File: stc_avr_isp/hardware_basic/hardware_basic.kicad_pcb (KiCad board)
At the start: 2 copper layers, 18 x 42.8 mm, 16 parts, among them J1 Conn_01x09_Socket, J2 Conn_01x09_Socket, J3 ISP, J4 BAUD RATE

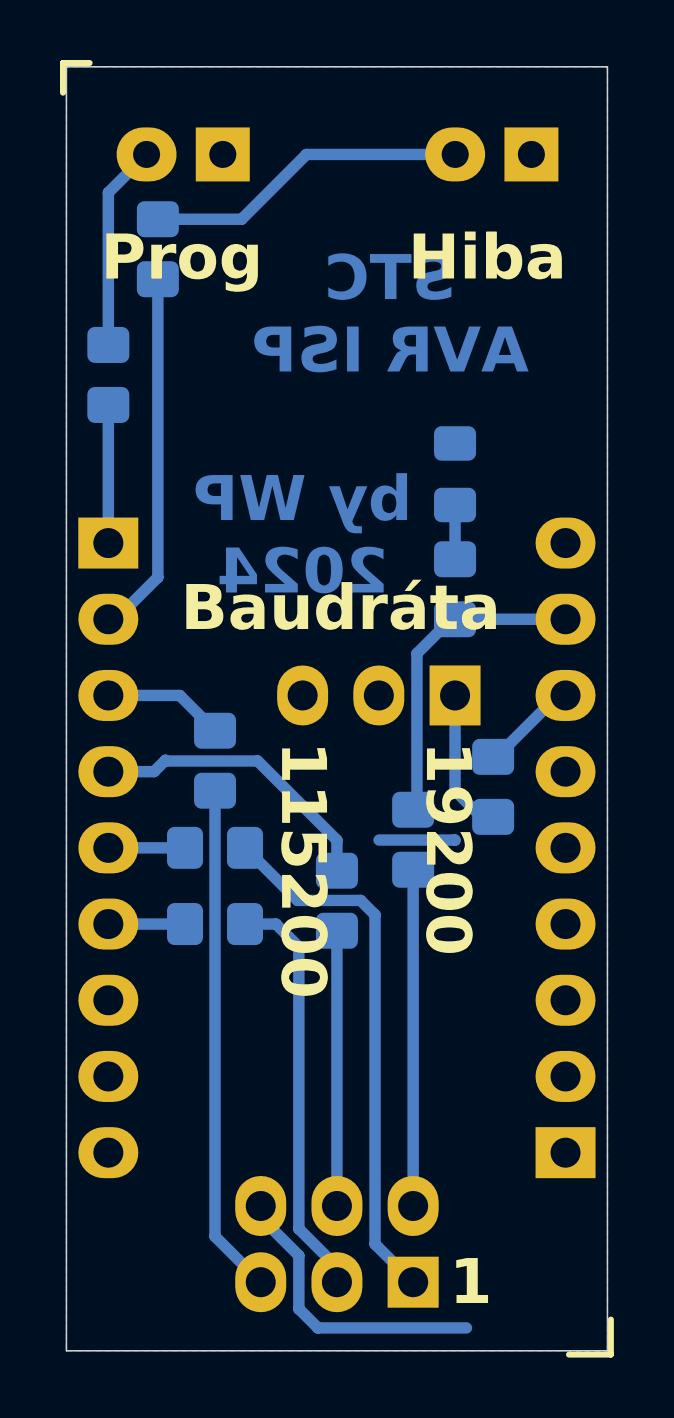
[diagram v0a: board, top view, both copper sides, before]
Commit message: Add fancy blink animation on reset, specify resistor values
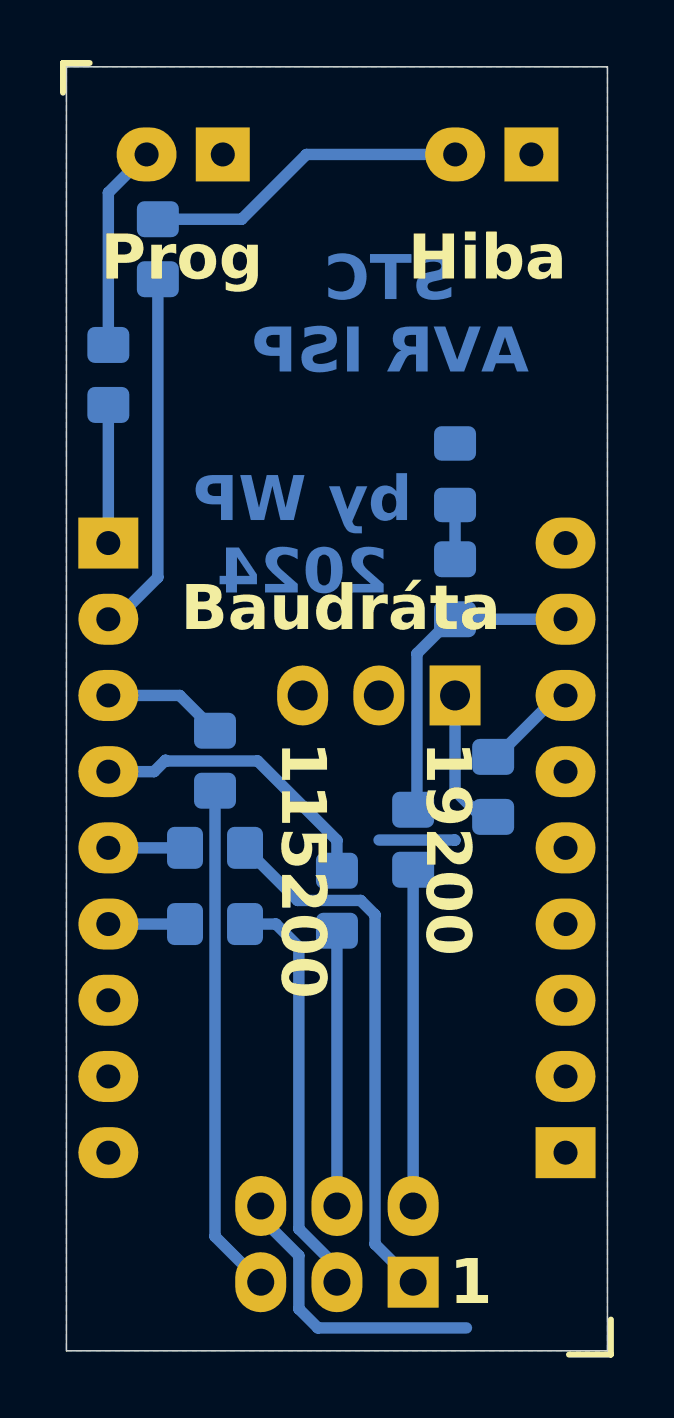
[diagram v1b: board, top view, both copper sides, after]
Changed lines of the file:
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@@
 			(at 0 0 180)
 			(size 1.8 1.8)
-			(drill 0.9)
+			(drill 0.8)
 			(layers "*.Cu" "*.Mask")
 			(remove_unused_layers no)
@@
 			(at 2.54 0 180)
 			(size 2 1.8)
-			(drill 0.9)
+			(drill 0.8)
 			(layers "*.Cu" "*.Mask")
 			(remove_unused_layers no)
@@
 			(at 0 0)
 			(size 2 1.7)
-			(drill 1)
+			(drill 0.8)
 			(layers "*.Cu" "*.Mask")
 			(remove_unused_layers no)
@@
 			(at 0 2.54)
 			(size 2 1.7)
-			(drill 1)
+			(drill 0.8)
 			(layers "*.Cu" "*.Mask")
 			(remove_unused_layers no)
@@
 			(at 0 5.08)
 			(size 2 1.7)
-			(drill 1)
+			(drill 0.8)
 			(layers "*.Cu" "*.Mask")
 			(remove_unused_layers no)
@@
 			(at 0 7.62)
 			(size 2 1.7)
-			(drill 1)
+			(drill 0.8)
 			(layers "*.Cu" "*.Mask")
 			(remove_unused_layers no)
@@
 			(at 0 10.16)
 			(size 2 1.7)
-			(drill 1)
+			(drill 0.8)
 			(layers "*.Cu" "*.Mask")
 			(remove_unused_layers no)
@@
 			(at 0 12.7)
 			(size 2 1.7)
-			(drill 1)
+			(drill 0.8)
 			(layers "*.Cu" "*.Mask")
 			(remove_unused_layers no)
@@
 			(at 0 15.24)
 			(size 2 1.7)
-			(drill 1)
+			(drill 0.8)
 			(layers "*.Cu" "*.Mask")
 			(remove_unused_layers no)
@@
 			(at 0 17.78)
 			(size 2 1.7)
-			(drill 1)
+			(drill 0.8)
 			(layers "*.Cu" "*.Mask")
 			(remove_unused_layers no)
@@
 			(at 0 20.32)
 			(size 2 1.7)
-			(drill 1)
+			(drill 0.8)
 			(layers "*.Cu" "*.Mask")
 			(remove_unused_layers no)
@@
 			(at 0 0 180)
 			(size 2 1.7)
-			(drill 1)
+			(drill 0.8)
 			(layers "*.Cu" "*.Mask")
 			(remove_unused_layers no)
@@
 			(at 0 2.54 180)
 			(size 2 1.7)
-			(drill 1)
+			(drill 0.8)
 			(layers "*.Cu" "*.Mask")
 			(remove_unused_layers no)
@@
 			(at 0 5.08 180)
 			(size 2 1.7)
-			(drill 1)
+			(drill 0.8)
 			(layers "*.Cu" "*.Mask")
 			(remove_unused_layers no)
@@
 			(at 0 7.62 180)
 			(size 2 1.7)
-			(drill 1)
+			(drill 0.8)
 			(layers "*.Cu" "*.Mask")
 			(remove_unused_layers no)
@@
 			(at 0 10.16 180)
 			(size 2 1.7)
-			(drill 1)
+			(drill 0.8)
 			(layers "*.Cu" "*.Mask")
 			(remove_unused_layers no)
@@
 			(at 0 12.7 180)
 			(size 2 1.7)
-			(drill 1)
+			(drill 0.8)
 			(layers "*.Cu" "*.Mask")
 			(remove_unused_layers no)
@@
 			(at 0 15.24 180)
 			(size 2 1.7)
-			(drill 1)
+			(drill 0.8)
 			(layers "*.Cu" "*.Mask")
 			(remove_unused_layers no)
@@
 			(at 0 17.78 180)
 			(size 2 1.7)
-			(drill 1)
+			(drill 0.8)
 			(layers "*.Cu" "*.Mask")
 			(remove_unused_layers no)
@@
 			(at 0 20.32 180)
 			(size 2 1.7)
-			(drill 1)
+			(drill 0.8)
 			(layers "*.Cu" "*.Mask")
 			(remove_unused_layers no)
@@
 			(at 0 0 180)
 			(size 1.8 1.8)
-			(drill 0.9)
+			(drill 0.8)
 			(layers "*.Cu" "*.Mask")
 			(remove_unused_layers no)
@@
 			(at 2.54 0 180)
 			(size 2 1.8)
-			(drill 0.9)
+			(drill 0.8)
 			(layers "*.Cu" "*.Mask")
 			(remove_unused_layers no)
@@
 			(at 0 0 90)
 			(size 2 1.7)
-			(drill 1)
+			(drill 0.9)
 			(layers "*.Cu" "*.Mask")
 			(remove_unused_layers no)
@@
 			(at -2.54 0 90)
 			(size 2 1.7)
-			(drill 1)
+			(drill 0.9)
 			(layers "*.Cu" "*.Mask")
 			(remove_unused_layers no)
@@
 			(at 0 2.54 90)
 			(size 2 1.7)
-			(drill 1)
+			(drill 0.9)
 			(layers "*.Cu" "*.Mask")
 			(remove_unused_layers no)
@@
 			(at -2.54 2.54 90)
 			(size 2 1.7)
-			(drill 1)
+			(drill 0.9)
 			(layers "*.Cu" "*.Mask")
 			(remove_unused_layers no)
@@
 			(at 0 5.08 90)
 			(size 2 1.7)
-			(drill 1)
+			(drill 0.9)
 			(layers "*.Cu" "*.Mask")
 			(remove_unused_layers no)
@@
 			(at -2.54 5.08 90)
 			(size 1.7 1.7)
-			(drill 1)
+			(drill 0.9)
 			(layers "*.Cu" "*.Mask")
 			(remove_unused_layers no)
@@
 		(tags "resistor handsolder")
 		(property "Reference" "R9"
-			(at 0 1.65 270)
+			(at 0 1.65 -90)
 			(layer "B.SilkS")
 			(effects
@@
 		)
 		(property "Value" "330"
-			(at 0 -1.65 270)
+			(at 0 -1.65 -90)
 			(layer "B.Fab")
 			(effects
@@
 		)
 		(fp_text user "${REFERENCE}"
-			(at 0 0 270)
+			(at 0 0 -90)
 			(layer "B.Fab")
 			(effects
@@
 		(tags "resistor handsolder")
 		(property "Reference" "R3"
-			(at 0 1.65 360)
+			(at 0 1.65 0)
 			(layer "B.SilkS")
 			(effects
@@
 		)
 		(property "Value" "100"
-			(at 0 -1.65 360)
+			(at 0 -1.65 0)
 			(layer "B.Fab")
 			(effects
@@
 		)
 		(fp_text user "${REFERENCE}"
-			(at 0 0 360)
+			(at 0 0 0)
 			(layer "B.Fab")
 			(effects
@@
 		(tags "resistor handsolder")
 		(property "Reference" "R4"
-			(at 0 1.65 360)
+			(at 0 1.65 0)
 			(layer "B.SilkS")
 			(effects
@@
 		)
 		(property "Value" "100"
-			(at 0 -1.65 360)
+			(at 0 -1.65 0)
 			(layer "B.Fab")
 			(effects
@@
 		)
 		(fp_text user "${REFERENCE}"
-			(at 0 0 360)
+			(at 0 0 0)
 			(layer "B.Fab")
 			(effects
